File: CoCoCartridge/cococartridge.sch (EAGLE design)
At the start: 52 parts, among them IC1 LPC1769, IC2 LD1117S33, IC3 DP83848C, P1 COCO-CART, Q1 BSS84, U1 USD-SOCKETNEW, X1 MINI-USB-UX60-MB-5ST

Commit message: First attempt at manual routing
Yet to be done:
* Get it reviewed by an actual EE.
* Clean up the component labels, etc.
* Verify component footprints.
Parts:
- P1: value COCO-CART -> COCO-CART3.5X2.5; device adam_custom:COCO-CART -> adam_custom:COCO-CART3.5X2.5
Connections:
- net N$1 renamed +5V
- net N$10 renamed USB_P
- net N$2 renamed USB2_P
- net N$7 renamed USB2_N
- net N$9 renamed USB_N
- net RD+ renamed RD_P
- net RD- renamed RD_N
- net TD+ renamed TD_P
- net TD- renamed TD_N
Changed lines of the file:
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@@
 <setting verticaltext="up"/>
 </settings>
-<grid distance="0.1" unitdist="inch" unit="inch" style="lines" multiple="1" display="yes" altdistance="0.01" altunitdist="inch" altunit="inch"/>
+<grid distance="0.1" unitdist="inch" unit="inch" style="lines" multiple="1" display="no" altdistance="0.01" altunitdist="inch" altunit="inch"/>
 <layers>
 <layer number="1" name="Top" color="4" fill="1" visible="no" active="no"/>
@@
 </variantdefs>
 <classes>
-<class number="0" name="default" width="0" drill="0">
+<class number="0" name="default" width="0.1524" drill="0">
+<clearance class="0" value="0.1524"/>
+</class>
+<class number="1" name="supply" width="0.1524" drill="0">
+<clearance class="1" value="0.1524"/>
+</class>
+<class number="2" name="io" width="0.1524" drill="0">
+<clearance class="2" value="0.1524"/>
+</class>
+<class number="3" name="usb" width="0.254" drill="0">
+<clearance class="3" value="0.1524"/>
+</class>
+<class number="4" name="ethernet" width="0.254" drill="0">
+<clearance class="4" value="0.1524"/>
 </class>
 </classes>
 <parts>
 <part name="IC1" library="lpc1xxx-v6" deviceset="LPC1769" device=""/>
-<part name="P1" library="adam_custom" deviceset="COCO-CART" device=""/>
+<part name="P1" library="adam_custom" deviceset="COCO-CART" device="3.5X2.5" value="COCO-CART3.5X2.5"/>
 <part name="SUPPLY2" library="supply2" deviceset="GND" device=""/>
 <part name="IC2" library="v-reg" deviceset="LD117A?*" device="S" technology="33TR" value="LD1117S33"/>
@@
 <part name="JP4" library="adam_custom" deviceset="JUMPER-1206" device="" value="JUMPER-1206"/>
 <part name="U$3" library="adam_custom" deviceset="CC-BY-SA-DOCFIELD" device=""/>
+<part name="+3V16" library="supply1" deviceset="+3V3" device=""/>
 </parts>
 <sheets>
@@
 <instance part="SUPPLY5" gate="GND" x="193.04" y="60.96"/>
 <instance part="+3V4" gate="G$1" x="172.72" y="76.2"/>
-<instance part="L1" gate="G$1" x="180.34" y="71.12" rot="R270"/>
+<instance part="L1" gate="G$1" x="180.34" y="71.12" smashed="yes" rot="R270">
+<attribute name="NAME" x="179.07" y="67.818" size="1.778" layer="95" rot="R270"/>
+<attribute name="VALUE" x="175.26" y="68.58" size="1.778" layer="96" rot="R270"/>
+</instance>
 <instance part="C7" gate="G$1" x="129.54" y="71.12"/>
 <instance part="U$1" gate="G$1" x="340.36" y="53.34" rot="R180"/>
@@
 <instance part="JP4" gate="G$1" x="363.22" y="83.82" rot="R90"/>
 <instance part="U$3" gate="G$1" x="27.94" y="177.8"/>
+<instance part="+3V16" gate="G$1" x="198.12" y="101.6"/>
 </instances>
 <busses>
 </busses>
 <nets>
-<net name="GND" class="0">
+<net name="GND" class="1">
 <segment>
 <pinref part="P1" gate="G$1" pin="GND@2"/>
@@
 </segment>
 </net>
-<net name="N$1" class="0">
+<net name="+5V" class="1">
 <segment>
 <pinref part="P1" gate="G$1" pin="+5V"/>
@@
 </segment>
 </net>
-<net name="+3V3" class="0">
+<net name="+3V3" class="1">
 <segment>
 <pinref part="IC2" gate="G$1" pin="OUT"/>
@@
 </segment>
 <segment>
-<pinref part="IC1" gate="G$1" pin="VDD(REG)(3V3)2"/>
 <pinref part="+3V3" gate="G$1" pin="+3V3"/>
-<wire x1="208.28" y1="83.82" x2="129.54" y2="83.82" width="0.1524" layer="91"/>
-<wire x1="129.54" y1="83.82" x2="129.54" y2="86.36" width="0.1524" layer="91"/>
-<pinref part="IC1" gate="G$1" pin="VDD(REG)(3V3)1"/>
-<wire x1="129.54" y1="86.36" x2="129.54" y2="88.9" width="0.1524" layer="91"/>
 <wire x1="129.54" y1="88.9" x2="129.54" y2="91.44" width="0.1524" layer="91"/>
 <wire x1="129.54" y1="91.44" x2="129.54" y2="93.98" width="0.1524" layer="91"/>
 <wire x1="129.54" y1="93.98" x2="129.54" y2="96.52" width="0.1524" layer="91"/>
 <wire x1="129.54" y1="96.52" x2="129.54" y2="99.06" width="0.1524" layer="91"/>
-<wire x1="208.28" y1="86.36" x2="129.54" y2="86.36" width="0.1524" layer="91"/>
-<junction x="129.54" y="86.36"/>
 <pinref part="IC1" gate="G$1" pin="VDD(3V3)4"/>
 <wire x1="208.28" y1="88.9" x2="160.02" y2="88.9" width="0.1524" layer="91"/>
@@
 <wire x1="137.16" y1="96.52" x2="129.54" y2="96.52" width="0.1524" layer="91"/>
 <wire x1="208.28" y1="78.74" x2="129.54" y2="78.74" width="0.1524" layer="91"/>
-<wire x1="129.54" y1="78.74" x2="129.54" y2="83.82" width="0.1524" layer="91"/>
-<junction x="129.54" y="83.82"/>
+<wire x1="129.54" y1="78.74" x2="129.54" y2="88.9" width="0.1524" layer="91"/>
 <pinref part="C5" gate="G$1" pin="1"/>
 <wire x1="137.16" y1="73.66" x2="137.16" y2="96.52" width="0.1524" layer="91"/>
@@
 <wire x1="434.34" y1="66.04" x2="434.34" y2="78.74" width="0.1524" layer="91"/>
 </segment>
+<segment>
+<pinref part="IC1" gate="G$1" pin="VDD(REG)(3V3)2"/>
+<wire x1="208.28" y1="83.82" x2="198.12" y2="83.82" width="0.1524" layer="91"/>
+<pinref part="+3V16" gate="G$1" pin="+3V3"/>
+<wire x1="198.12" y1="83.82" x2="198.12" y2="86.36" width="0.1524" layer="91"/>
+<pinref part="IC1" gate="G$1" pin="VDD(REG)(3V3)1"/>
+<wire x1="198.12" y1="86.36" x2="198.12" y2="99.06" width="0.1524" layer="91"/>
+<wire x1="208.28" y1="86.36" x2="198.12" y2="86.36" width="0.1524" layer="91"/>
+<junction x="198.12" y="86.36"/>
+</segment>
 </net>
 <net name="!RESET" class="0">
@@
 </segment>
 </net>
-<net name="N$2" class="0">
+<net name="USB2_P" class="3">
 <segment>
 <pinref part="X1" gate="G$1" pin="3"/>
@@
 </segment>
 </net>
-<net name="N$7" class="0">
+<net name="USB2_N" class="3">
 <segment>
 <pinref part="X1" gate="G$1" pin="2"/>
@@
 </segment>
 </net>
-<net name="N$9" class="0">
+<net name="USB_N" class="3">
 <segment>
 <pinref part="R7" gate="G$1" pin="2"/>
@@
 </segment>
 </net>
-<net name="N$10" class="0">
+<net name="USB_P" class="3">
 <segment>
 <pinref part="R6" gate="G$1" pin="2"/>
@@
 </segment>
 </net>
-<net name="RD-" class="0">
+<net name="RD_N" class="4">
 <segment>
 <pinref part="IC3" gate="G$1" pin="RD-"/>
@@
 </segment>
 </net>
-<net name="RD+" class="0">
+<net name="RD_P" class="4">
 <segment>
 <pinref part="IC3" gate="G$1" pin="RD+"/>
@@
 </segment>
 </net>
-<net name="TD-" class="0">
+<net name="TD_N" class="4">
 <segment>
 <pinref part="IC3" gate="G$1" pin="TD-"/>
@@
 </segment>
 </net>
-<net name="TD+" class="0">
+<net name="TD_P" class="4">
 <segment>
 <pinref part="IC3" gate="G$1" pin="TD+"/>

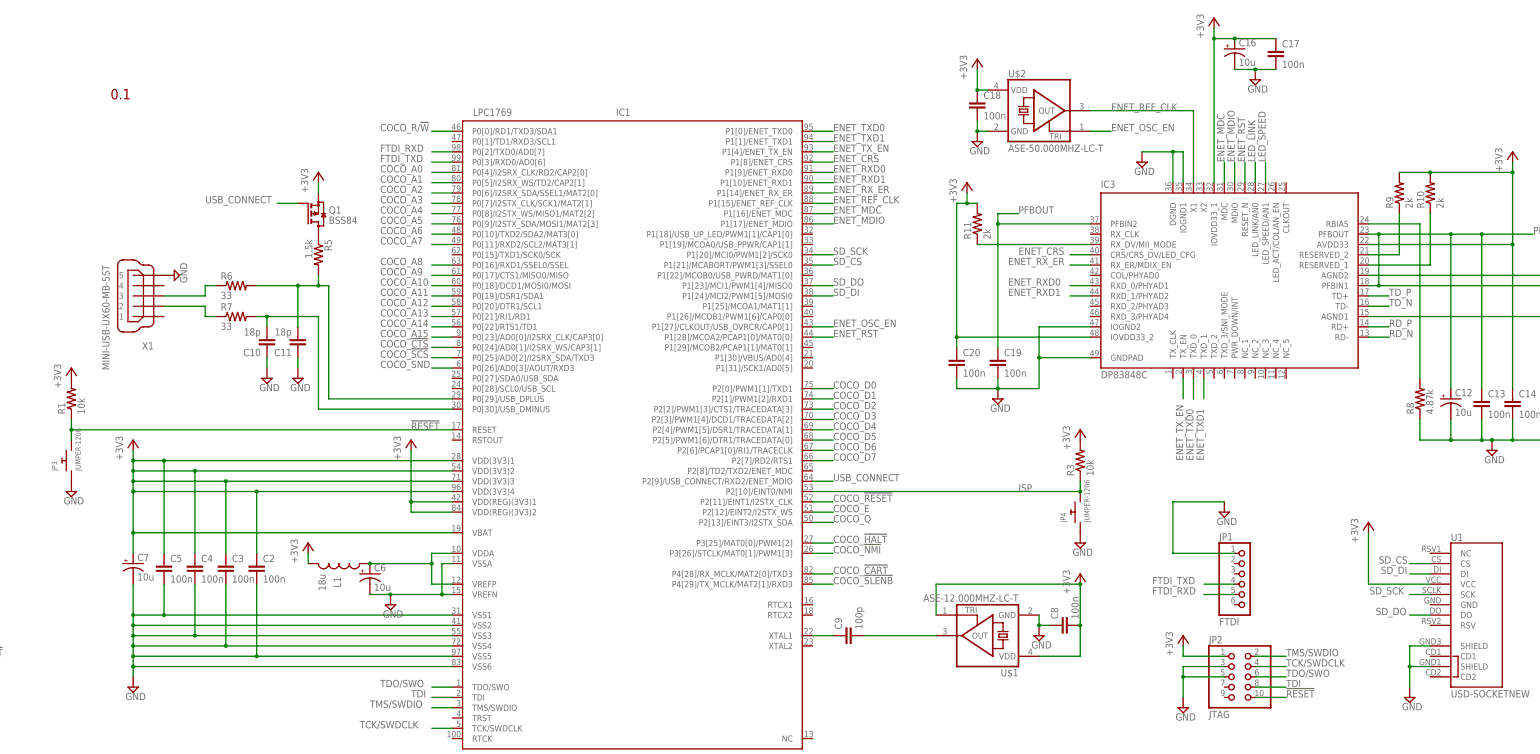
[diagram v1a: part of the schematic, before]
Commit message: Revision 1.0 sent to OSHPark
This is the first version that I sent off to OSHPark for manufacturing
tonight.
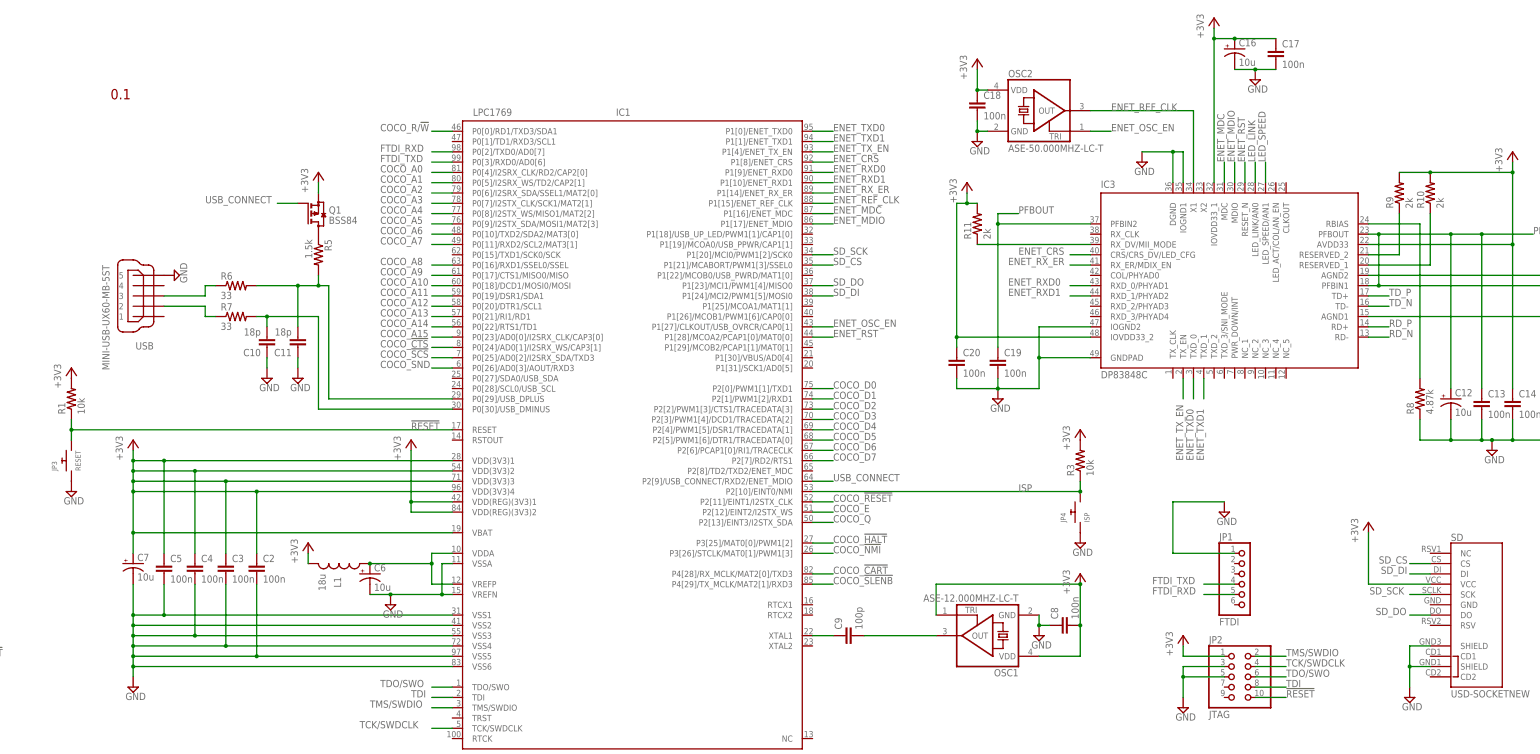
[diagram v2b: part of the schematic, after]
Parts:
- JP3: value JUMPER-1206 -> RESET
- JP4: value JUMPER-1206 -> ISP
- renumbered U$1 to OSC1, U$2 to OSC2, U1 to SD, X1 to USB
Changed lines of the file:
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@@
 <part name="L1" library="SparkFun-Passives" deviceset="INDUCTOR" device="1210" value="18u"/>
 <part name="C7" library="SparkFun-Capacitors" deviceset="CAP_POL" device="1206" value="10u"/>
-<part name="U$1" library="crystal" deviceset="ASE" device="" value="ASE-12.000MHZ-LC-T"/>
+<part name="OSC1" library="crystal" deviceset="ASE" device="" value="ASE-12.000MHZ-LC-T"/>
 <part name="SUPPLY6" library="supply2" deviceset="GND" device=""/>
 <part name="+3V5" library="supply1" deviceset="+3V3" device=""/>
@@
 <part name="SUPPLY9" library="supply2" deviceset="GND" device=""/>
 <part name="Q1" library="transistor-small-signal" deviceset="BSS84" device=""/>
-<part name="X1" library="con-hirose" deviceset="MINI-USB-" device="UX60-MB-5ST"/>
+<part name="USB" library="con-hirose" deviceset="MINI-USB-" device="UX60-MB-5ST"/>
 <part name="SUPPLY10" library="supply2" deviceset="GND" device=""/>
 <part name="R5" library="SparkFun-Resistors" deviceset="RESISTOR" device="0805-RES" value="1.5k"/>
@@
 <part name="C17" library="SparkFun-Passives" deviceset="CAP" device="0805" value="100n"/>
 <part name="SUPPLY15" library="supply2" deviceset="GND" device=""/>
-<part name="U$2" library="crystal" deviceset="ASE" device="" value="ASE-50.000MHZ-LC-T"/>
+<part name="OSC2" library="crystal" deviceset="ASE" device="" value="ASE-50.000MHZ-LC-T"/>
 <part name="+3V11" library="supply1" deviceset="+3V3" device=""/>
 <part name="C18" library="SparkFun-Passives" deviceset="CAP" device="0805" value="100n"/>
@@
 <part name="R17" library="SparkFun-Resistors" deviceset="RESISTOR" device="0805-RES" value="270"/>
 <part name="+3V13" library="supply1" deviceset="+3V3" device=""/>
-<part name="U1" library="adam_custom" deviceset="USD-SOCKET" device="NEW"/>
+<part name="SD" library="adam_custom" deviceset="USD-SOCKET" device="NEW"/>
 <part name="SUPPLY17" library="supply2" deviceset="GND" device=""/>
 <part name="+3V15" library="supply1" deviceset="+3V3" device=""/>
 <part name="C6" library="SparkFun-Capacitors" deviceset="CAP_POL" device="1206" value="10u"/>
-<part name="JP3" library="adam_custom" deviceset="JUMPER-1206" device="" value="JUMPER-1206"/>
-<part name="JP4" library="adam_custom" deviceset="JUMPER-1206" device="" value="JUMPER-1206"/>
+<part name="JP3" library="adam_custom" deviceset="JUMPER-1206" device="" value="RESET"/>
+<part name="JP4" library="adam_custom" deviceset="JUMPER-1206" device="" value="ISP"/>
 <part name="U$3" library="adam_custom" deviceset="CC-BY-SA-DOCFIELD" device=""/>
 <part name="+3V16" library="supply1" deviceset="+3V3" device=""/>
@@
 </instance>
 <instance part="C7" gate="G$1" x="129.54" y="71.12"/>
-<instance part="U$1" gate="G$1" x="340.36" y="53.34" rot="R180"/>
+<instance part="OSC1" gate="G$1" x="340.36" y="53.34" rot="R180"/>
 <instance part="SUPPLY6" gate="GND" x="353.06" y="53.34"/>
 <instance part="+3V5" gate="G$1" x="363.22" y="68.58"/>
@@
 <instance part="SUPPLY9" gate="GND" x="388.62" y="35.56"/>
 <instance part="Q1" gate="G$1" x="175.26" y="157.48"/>
-<instance part="X1" gate="G$1" x="132.08" y="137.16" rot="R180"/>
+<instance part="USB" gate="G$1" x="132.08" y="137.16" rot="R180"/>
 <instance part="SUPPLY10" gate="GND" x="139.7" y="142.24" rot="R90"/>
 <instance part="R5" gate="G$1" x="175.26" y="147.32" rot="R270"/>
@@
 <instance part="C17" gate="G$1" x="411.48" y="195.58"/>
 <instance part="SUPPLY15" gate="GND" x="406.4" y="190.5"/>
-<instance part="U$2" gate="G$1" x="353.06" y="182.88"/>
+<instance part="OSC2" gate="G$1" x="353.06" y="182.88"/>
 <instance part="+3V11" gate="G$1" x="337.82" y="195.58"/>
 <instance part="C18" gate="G$1" x="337.82" y="182.88"/>
@@
 <instance part="R17" gate="G$1" x="594.36" y="160.02" rot="R90"/>
 <instance part="+3V13" gate="G$1" x="589.28" y="170.18"/>
-<instance part="U1" gate="G$1" x="457.2" y="60.96"/>
+<instance part="SD" gate="G$1" x="457.2" y="60.96"/>
 <instance part="SUPPLY17" gate="GND" x="444.5" y="38.1"/>
 <instance part="+3V15" gate="G$1" x="434.34" y="81.28"/>
@@
 </segment>
 <segment>
-<pinref part="U$1" gate="G$1" pin="GND"/>
+<pinref part="OSC1" gate="G$1" pin="GND"/>
 <pinref part="SUPPLY6" gate="GND" pin="GND"/>
 <wire x1="353.06" y1="55.88" x2="353.06" y2="58.42" width="0.1524" layer="91"/>
@@
 </segment>
 <segment>
-<pinref part="X1" gate="G$1" pin="5"/>
+<pinref part="USB" gate="G$1" pin="5"/>
 <pinref part="SUPPLY10" gate="GND" pin="GND"/>
 </segment>
@@
 <pinref part="SUPPLY16" gate="GND" pin="GND"/>
 <wire x1="337.82" y1="180.34" x2="337.82" y2="177.8" width="0.1524" layer="91"/>
-<pinref part="U$2" gate="G$1" pin="GND"/>
+<pinref part="OSC2" gate="G$1" pin="GND"/>
 <wire x1="337.82" y1="177.8" x2="340.36" y2="177.8" width="0.1524" layer="91"/>
 <junction x="337.82" y="177.8"/>
@@
 </segment>
 <segment>
-<pinref part="U1" gate="G$1" pin="SHIELD@3"/>
+<pinref part="SD" gate="G$1" pin="SHIELD@3"/>
 <pinref part="SUPPLY17" gate="GND" pin="GND"/>
 <wire x1="449.58" y1="45.72" x2="444.5" y2="45.72" width="0.1524" layer="91"/>
 <wire x1="444.5" y1="45.72" x2="444.5" y2="40.64" width="0.1524" layer="91"/>
-<pinref part="U1" gate="G$1" pin="SHIELD@1"/>
+<pinref part="SD" gate="G$1" pin="SHIELD@1"/>
 <wire x1="449.58" y1="50.8" x2="444.5" y2="50.8" width="0.1524" layer="91"/>
 <wire x1="444.5" y1="50.8" x2="444.5" y2="45.72" width="0.1524" layer="91"/>
@@
 </segment>
 <segment>
-<pinref part="U$1" gate="G$1" pin="VDD"/>
+<pinref part="OSC1" gate="G$1" pin="VDD"/>
 <pinref part="+3V5" gate="G$1" pin="+3V3"/>
 <wire x1="353.06" y1="48.26" x2="363.22" y2="48.26" width="0.1524" layer="91"/>
@@
 <wire x1="363.22" y1="55.88" x2="363.22" y2="66.04" width="0.1524" layer="91"/>
 <junction x="363.22" y="55.88"/>
-<pinref part="U$1" gate="G$1" pin="TRI"/>
+<pinref part="OSC1" gate="G$1" pin="TRI"/>
 <wire x1="327.66" y1="58.42" x2="327.66" y2="66.04" width="0.1524" layer="91"/>
 <wire x1="327.66" y1="66.04" x2="363.22" y2="66.04" width="0.1524" layer="91"/>
@@
 </segment>
 <segment>
-<pinref part="U$2" gate="G$1" pin="VDD"/>
+<pinref part="OSC2" gate="G$1" pin="VDD"/>
 <pinref part="+3V11" gate="G$1" pin="+3V3"/>
 <wire x1="340.36" y1="187.96" x2="337.82" y2="187.96" width="0.1524" layer="91"/>
@@
 </segment>
 <segment>
-<pinref part="U1" gate="G$1" pin="VCC"/>
+<pinref part="SD" gate="G$1" pin="VCC"/>
 <pinref part="+3V15" gate="G$1" pin="+3V3"/>
 <wire x1="449.58" y1="66.04" x2="434.34" y2="66.04" width="0.1524" layer="91"/>
@@
 <segment>
 <pinref part="C9" gate="G$1" pin="2"/>
-<pinref part="U$1" gate="G$1" pin="OUT"/>
+<pinref part="OSC1" gate="G$1" pin="OUT"/>
 <wire x1="309.88" y1="53.34" x2="327.66" y2="53.34" width="0.1524" layer="91"/>
 </segment>
@@
 <net name="USB2_P" class="3">
 <segment>
-<pinref part="X1" gate="G$1" pin="3"/>
+<pinref part="USB" gate="G$1" pin="3"/>
 <wire x1="137.16" y1="137.16" x2="147.32" y2="137.16" width="0.1524" layer="91"/>
 <wire x1="147.32" y1="137.16" x2="147.32" y2="139.7" width="0.1524" layer="91"/>
@@
 <net name="USB2_N" class="3">
 <segment>
-<pinref part="X1" gate="G$1" pin="2"/>
+<pinref part="USB" gate="G$1" pin="2"/>
 <wire x1="137.16" y1="134.62" x2="147.32" y2="134.62" width="0.1524" layer="91"/>
 <pinref part="R7" gate="G$1" pin="1"/>
@@
 </segment>
 <segment>
-<pinref part="U$2" gate="G$1" pin="OUT"/>
+<pinref part="OSC2" gate="G$1" pin="OUT"/>
 <pinref part="IC3" gate="G$1" pin="X1"/>
 <wire x1="365.76" y1="182.88" x2="391.16" y2="182.88" width="0.1524" layer="91"/>
@@
 </segment>
 <segment>
-<pinref part="U$2" gate="G$1" pin="TRI"/>
+<pinref part="OSC2" gate="G$1" pin="TRI"/>
 <wire x1="365.76" y1="177.8" x2="370.84" y2="177.8" width="0.1524" layer="91"/>
 <label x="370.84" y="177.8" size="1.778" layer="95"/>
@@
 </segment>
 <segment>
-<pinref part="U1" gate="G$1" pin="SCK"/>
+<pinref part="SD" gate="G$1" pin="SCK"/>
 <wire x1="449.58" y1="63.5" x2="444.5" y2="63.5" width="0.1524" layer="91"/>
 <label x="434.594" y="63.5" size="1.778" layer="95"/>
@@
 </segment>
 <segment>
-<pinref part="U1" gate="G$1" pin="CS"/>
+<pinref part="SD" gate="G$1" pin="CS"/>
 <wire x1="449.58" y1="71.12" x2="444.5" y2="71.12" width="0.1524" layer="91"/>
 <label x="436.88" y="71.12" size="1.778" layer="95"/>
@@
 </segment>
 <segment>
-<pinref part="U1" gate="G$1" pin="DO"/>
+<pinref part="SD" gate="G$1" pin="DO"/>
 <wire x1="449.58" y1="58.42" x2="444.5" y2="58.42" width="0.1524" layer="91"/>
 <label x="436.118" y="58.42" size="1.778" layer="95"/>
@@
 </segment>
 <segment>
-<pinref part="U1" gate="G$1" pin="DI"/>
+<pinref part="SD" gate="G$1" pin="DI"/>
 <wire x1="449.58" y1="68.58" x2="444.5" y2="68.58" width="0.1524" layer="91"/>
 <label x="437.388" y="68.58" size="1.778" layer="95"/>
